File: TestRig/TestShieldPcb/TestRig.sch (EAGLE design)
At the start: 7 parts, among them J1 POWER_JACKPTH, U1 ARDUINO_SHIELDNOHOLES

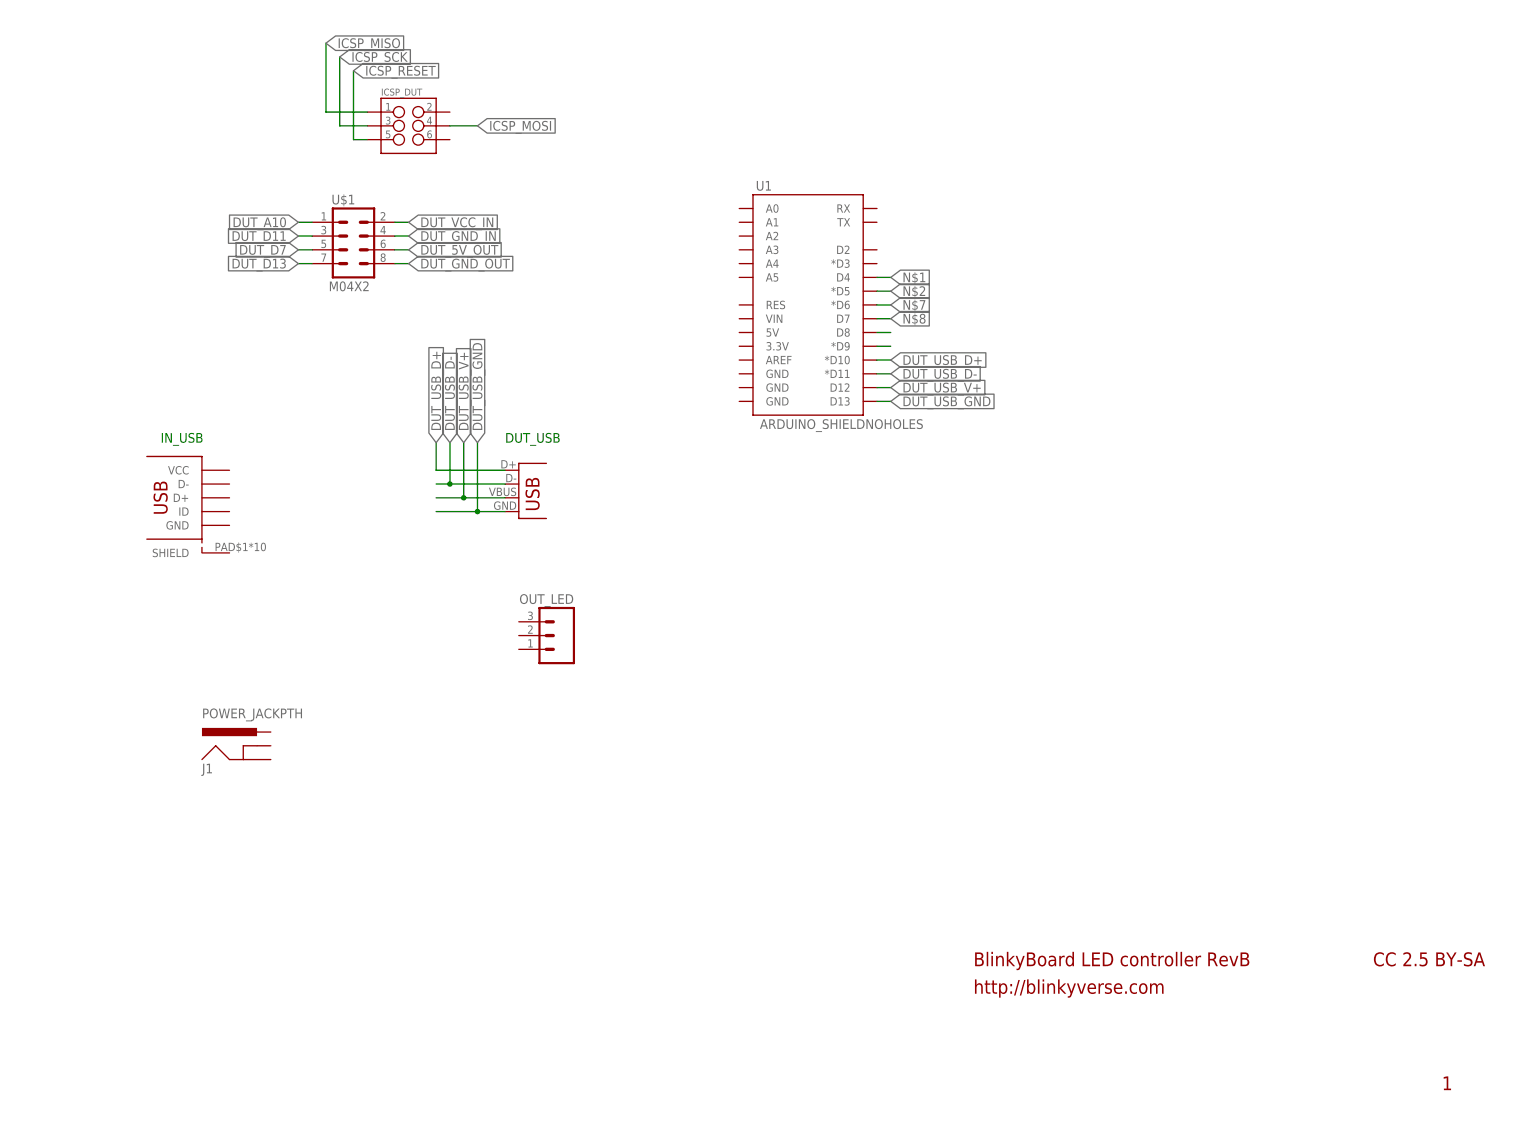
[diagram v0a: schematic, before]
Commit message: Add test shield design
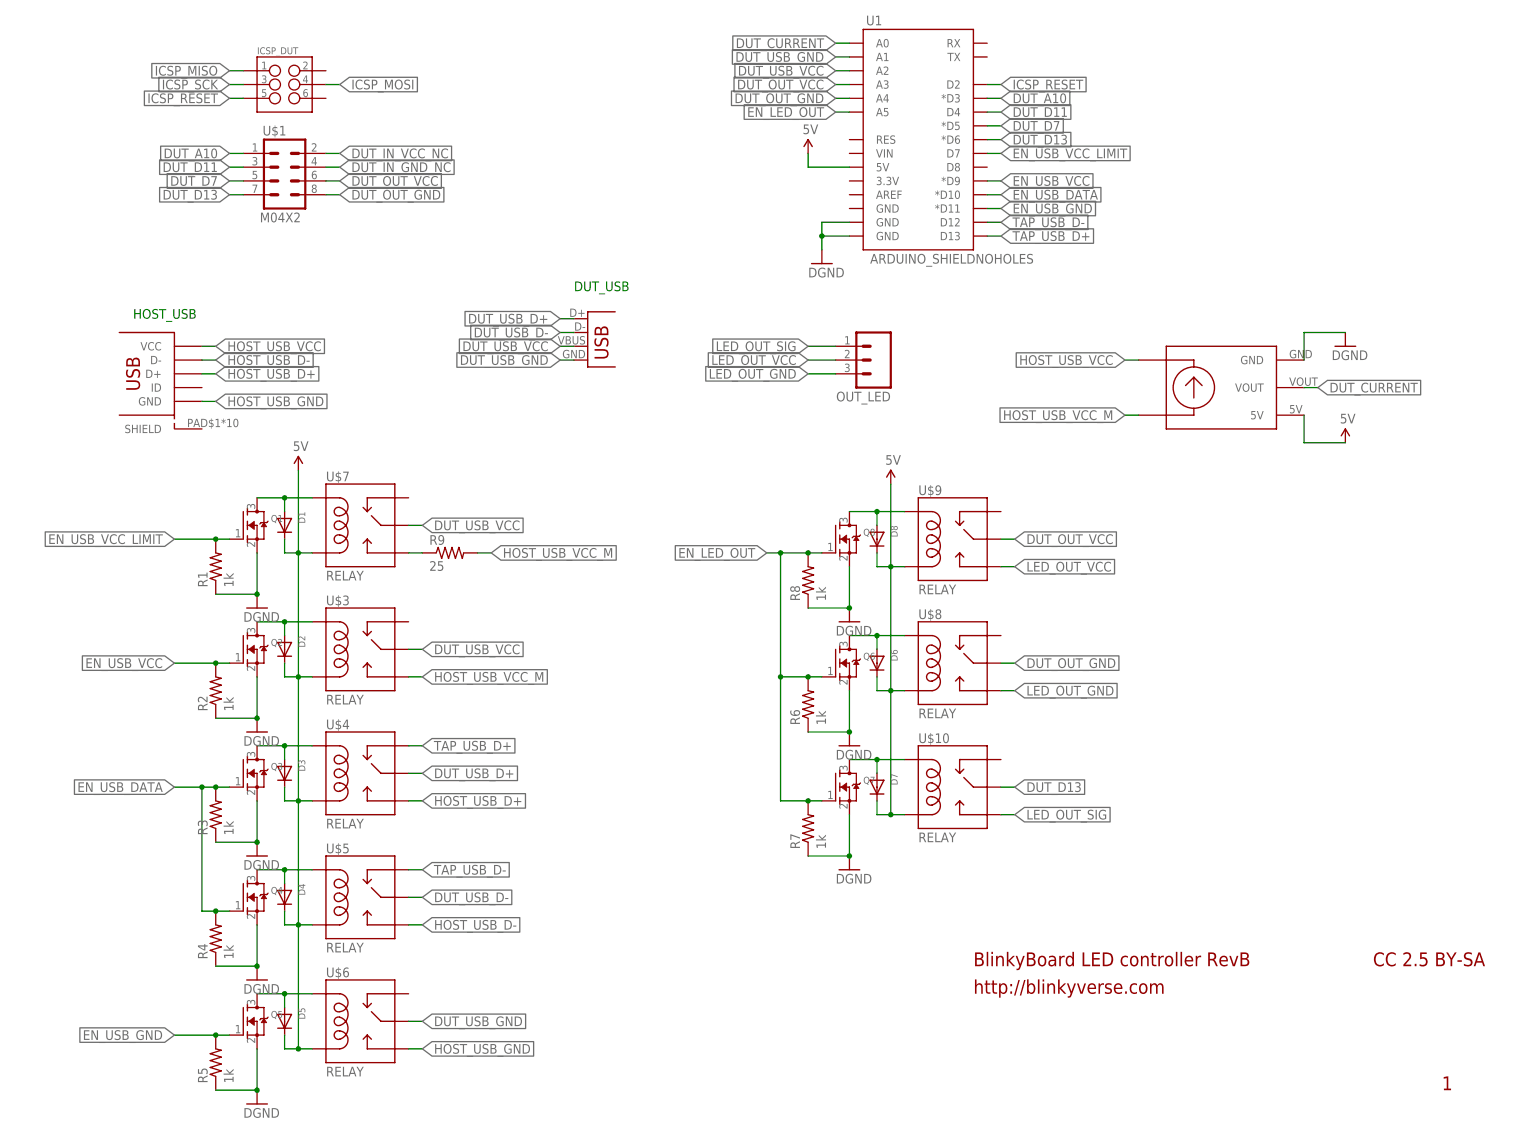
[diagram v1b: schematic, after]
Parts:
- removed J1: POWER_JACKPTH, SparkFun-Connectors:POWER_JACKPTH
- added D1, D2, D3, D4, D5, D6, D7, D8: (no value), adafruit:DIODESOD-523
- added Q1, Q2, Q3, Q4, Q5, Q6, Q7, Q8: (no value), adafruit:MOSFET-NREFLOW
- added R1, R2, R3, R4, R5, R6, R7, R8: 1k, adafruit:R-US_R0603
- added R9: 25, adafruit:R-US_R1210
- added U$10, U$3, U$4, U$5, U$6, U$7, U$8, U$9: RELAY, blinkiverse:RELAY
- added U$11: SPARKFUN_ACS712, blinkiverse:SPARKFUN_ACS712
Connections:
- net DUT_GND_IN renamed DUT_IN_GND_NC
- net DUT_VCC_IN renamed DUT_IN_VCC_NC
- removed net DUT_5V_OUT: U$1.6
- removed net DUT_GND_OUT: U$1.8
- removed net DUT_USB_V+: JP1.VBUS, U1.D12
- removed net N$1: U1.D4
- removed net N$10: U1.*D9
- removed net N$2: U1.*D5
- removed net N$7: U1.*D6
- removed net N$8: U1.D7
- new net 5V: D1.C, D2.C, D3.C, D4.C, D5.C, D6.C, D7.C, D8.C, U$10.COIL2, U$11.5V, U$3.COIL2, U$4.COIL2, U$5.COIL2, U$6.COIL2, U$7.COIL2, U$8.COIL2, U$9.COIL2, U1.5V
- new net DUT_CURRENT: U$11.VOUT, U1.A0
- new net DUT_OUT_GND: U$1.8, U$8.MAIN, U1.A4
- new net DUT_OUT_VCC: U$1.6, U$9.MAIN, U1.A3
- new net DUT_USB_VCC: JP1.VBUS, U$3.MAIN, U$7.MAIN, U1.A2
- new net EN_LED_OUT: Q6.G, Q7.G, Q8.G, R6.2, R7.2, R8.2, U1.A5
- new net EN_USB_DATA: Q3.G, Q4.G, R3.2, R4.2, U1.*D10
- new net EN_USB_GND: Q5.G, R5.2, U1.*D11
- new net EN_USB_VCC: Q2.G, R2.2, U1.*D9
- new net EN_USB_VCC_LIMIT: Q1.G, R1.2, U1.D7
- new net GND: Q1.S, Q2.S, Q3.S, Q4.S, Q5.S, Q6.S, Q7.S, Q8.S, R1.1, R2.1, R3.1, R4.1, R5.1, R6.1, R7.1, R8.1, U$11.GND, U1.GND@0, U1.GND@1
- new net HOST_USB_D+: U$2.D+, U$4.NO
- new net HOST_USB_D-: U$2.D-, U$5.NO
- new net HOST_USB_GND: U$2.GND, U$6.NO
- new net HOST_USB_VCC: U$11.IP+, U$2.VCC
- new net HOST_USB_VCC_M: R9.2, U$11.IP-, U$3.NO
- new net LED_OUT_GND: OUT_LED.3, U$8.NO
- new net LED_OUT_SIG: OUT_LED.1, U$10.NO
- new net LED_OUT_VCC: OUT_LED.2, U$9.NO
- new net N$14: D1.A, Q1.D, U$7.COIL1
- new net N$20: D2.A, Q2.D, U$3.COIL1
- new net N$27: D3.A, Q3.D, U$4.COIL1
- new net N$31: D4.A, Q4.D, U$5.COIL1
- new net N$35: D5.A, Q5.D, U$6.COIL1
- new net N$38: D6.A, Q6.D, U$8.COIL1
- new net N$42: D7.A, Q7.D, U$10.COIL1
- new net N$46: D8.A, Q8.D, U$9.COIL1
- new net TAP_USB_D+: U$4.NC, U1.D13
- new net TAP_USB_D-: U$5.NC, U1.D12
- net DUT_A10: now also U1.*D3
- net DUT_D11: now also U1.D4
- net DUT_D13: now also U$10.MAIN, U1.*D6
- net DUT_D7: now also U1.*D5
- net DUT_USB_D+: now also U$4.MAIN; no longer U1.*D10
- net DUT_USB_D-: now also U$5.MAIN; no longer U1.*D11
- net DUT_USB_GND: now also U$6.MAIN, U1.A1; no longer U1.D13
- net ICSP_RESET: now also U1.D2
- net N$9: now also R9.1, U$7.NO; no longer U1.D8
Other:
- note added: "HOST_USB"
- note removed: "IN_USB"
- moved on the sheet: ICSP_DUT, OUT_LED, U$1, U1

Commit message: RevD of the test shield PCB
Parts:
- removed JP1: USB-A-SMD, SparkFun-Connectors:USB-A-SMD
- added TEST_DUT: M04X2, SparkFun-Connectors:M04X2
- U$1: value M04X2 -> USB; device SparkFun-Connectors:M04X2 -> blinkiverse:USB
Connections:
- new net DUT_USB_SHIELD: U$1.SHIELD, U1.D7
- net DUT_A10: now also TEST_DUT.1; no longer U$1.1
- net DUT_D11: now also TEST_DUT.3; no longer U$1.3
- net DUT_D13: now also TEST_DUT.7; no longer U$1.7
- net DUT_D7: now also TEST_DUT.5; no longer U$1.5
- net DUT_IN_GND_NC: now also TEST_DUT.4; no longer U$1.4
- net DUT_IN_VCC_NC: now also TEST_DUT.2; no longer U$1.2
- net DUT_OUT_GND: now also TEST_DUT.8; no longer U$1.8
- net DUT_OUT_VCC: now also TEST_DUT.6; no longer U$1.6
- net DUT_USB_D+: now also U$1.D+; no longer JP1.D+
- net DUT_USB_D-: now also U$1.D-; no longer JP1.D-
- net DUT_USB_GND: now also U$1.GND; no longer JP1.GND
- net DUT_USB_VCC: now also U$1.VCC; no longer JP1.VBUS
- net EN_USB_VCC_LIMIT: now also U1.D8; no longer U1.D7
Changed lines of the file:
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@@
 <part name="FRAME1" library="frames" deviceset="FRAME_A_L" device=""/>
 <part name="ICSP_DUT" library="SparkFun-Connectors" deviceset="M03X2" device="NO_SILK"/>
-<part name="JP1" library="SparkFun-Connectors" deviceset="USB" device="-A-SMD" value="USB-A-SMD"/>
 <part name="OUT_LED" library="SparkFun-Connectors" deviceset="M03" device="PTH"/>
 <part name="U1" library="SparkFun-Boards" deviceset="ARDUINO_SHIELD" device="NOHOLES"/>
-<part name="U$1" library="SparkFun-Connectors" deviceset="M04X2" device=""/>
+<part name="TEST_DUT" library="SparkFun-Connectors" deviceset="M04X2" device=""/>
 <part name="U$2" library="blinkiverse" deviceset="MICRO_USB" device="SMT+THRUHULE"/>
 <part name="U$3" library="blinkiverse" deviceset="RELAY" device=""/>
@@
 <part name="GND10" library="SparkFun-Aesthetics" deviceset="DGND" device=""/>
 <part name="SUPPLY4" library="SparkFun-Aesthetics" deviceset="5V" device=""/>
+<part name="U$1" library="blinkiverse" deviceset="USB" device=""/>
 </parts>
 <sheets>
@@
 <text x="177.8" y="-30.48" size="2.54" layer="94">CC 2.5 BY-SA</text>
 <text x="190.5" y="-53.34" size="2.54" layer="94">1</text>
-<text x="30.48" y="93.98" size="1.778" layer="91">DUT_USB</text>
+<text x="20.32" y="88.9" size="1.778" layer="91">DUT_USB</text>
 <text x="-50.8" y="88.9" size="1.778" layer="91">HOST_USB</text>
 </plain>
@@
 <instance part="FRAME1" gate="G$2" x="101.6" y="-60.96"/>
 <instance part="ICSP_DUT" gate="G$1" x="-22.86" y="132.08"/>
-<instance part="JP1" gate="G$1" x="33.02" y="81.28"/>
 <instance part="OUT_LED" gate="G$1" x="86.36" y="81.28" rot="R180"/>
 <instance part="U1" gate="G$1" x="93.98" y="121.92"/>
-<instance part="U$1" gate="G$1" x="-22.86" y="114.3"/>
+<instance part="TEST_DUT" gate="G$1" x="-22.86" y="114.3"/>
 <instance part="U$2" gate="G$1" x="-45.72" y="78.74"/>
 <instance part="U$3" gate="G$1" x="-7.62" y="27.94"/>
@@
 <instance part="GND10" gate="G$1" x="172.72" y="83.82"/>
 <instance part="SUPPLY4" gate="G$1" x="172.72" y="66.04"/>
+<instance part="U$1" gate="G$1" x="35.56" y="78.74" rot="MR0"/>
 </instances>
 <busses>
@@
 <net name="DUT_A10" class="0">
 <segment>
-<pinref part="U$1" gate="G$1" pin="1"/>
+<pinref part="TEST_DUT" gate="G$1" pin="1"/>
 <wire x1="-30.48" y1="119.38" x2="-33.02" y2="119.38" width="0.1524" layer="91"/>
 <label x="-33.02" y="119.38" size="1.778" layer="95" rot="R180" xref="yes"/>
@@
 <net name="DUT_D11" class="0">
 <segment>
-<pinref part="U$1" gate="G$1" pin="3"/>
+<pinref part="TEST_DUT" gate="G$1" pin="3"/>
 <wire x1="-33.02" y1="116.84" x2="-30.48" y2="116.84" width="0.1524" layer="91"/>
 <label x="-33.02" y="116.84" size="1.778" layer="95" rot="R180" xref="yes"/>
@@
 <net name="DUT_D7" class="0">
 <segment>
-<pinref part="U$1" gate="G$1" pin="5"/>
+<pinref part="TEST_DUT" gate="G$1" pin="5"/>
 <wire x1="-33.02" y1="114.3" x2="-30.48" y2="114.3" width="0.1524" layer="91"/>
 <label x="-33.02" y="114.3" size="1.778" layer="95" rot="R180" xref="yes"/>
@@
 <net name="DUT_D13" class="0">
 <segment>
-<pinref part="U$1" gate="G$1" pin="7"/>
+<pinref part="TEST_DUT" gate="G$1" pin="7"/>
 <wire x1="-33.02" y1="111.76" x2="-30.48" y2="111.76" width="0.1524" layer="91"/>
 <label x="-33.02" y="111.76" size="1.778" layer="95" rot="R180" xref="yes"/>
@@
 <net name="DUT_IN_VCC_NC" class="0">
 <segment>
-<pinref part="U$1" gate="G$1" pin="2"/>
+<pinref part="TEST_DUT" gate="G$1" pin="2"/>
 <wire x1="-15.24" y1="119.38" x2="-12.7" y2="119.38" width="0.1524" layer="91"/>
 <label x="-12.7" y="119.38" size="1.778" layer="95" xref="yes"/>
@@
 <net name="DUT_IN_GND_NC" class="0">
 <segment>
-<pinref part="U$1" gate="G$1" pin="4"/>
+<pinref part="TEST_DUT" gate="G$1" pin="4"/>
 <wire x1="-15.24" y1="116.84" x2="-12.7" y2="116.84" width="0.1524" layer="91"/>
 <label x="-12.7" y="116.84" size="1.778" layer="95" xref="yes"/>
@@
 <net name="DUT_OUT_GND" class="0">
 <segment>
-<pinref part="U$1" gate="G$1" pin="8"/>
+<pinref part="TEST_DUT" gate="G$1" pin="8"/>
 <wire x1="-15.24" y1="111.76" x2="-12.7" y2="111.76" width="0.1524" layer="91"/>
 <label x="-12.7" y="111.76" size="1.778" layer="95" xref="yes"/>
@@
 <net name="DUT_USB_D+" class="0">
 <segment>
-<pinref part="JP1" gate="G$1" pin="D+"/>
-<wire x1="30.48" y1="88.9" x2="27.94" y2="88.9" width="0.1524" layer="91"/>
-<label x="27.94" y="88.9" size="1.778" layer="95" rot="R180" xref="yes"/>
+<label x="22.86" y="78.74" size="1.778" layer="95" rot="R180" xref="yes"/>
+<pinref part="U$1" gate="G$1" pin="D+"/>
+<wire x1="22.86" y1="78.74" x2="27.94" y2="78.74" width="0.1524" layer="91"/>
 </segment>
 <segment>
@@
 <net name="DUT_USB_D-" class="0">
 <segment>
-<pinref part="JP1" gate="G$1" pin="D-"/>
-<wire x1="30.48" y1="86.36" x2="27.94" y2="86.36" width="0.1524" layer="91"/>
-<label x="27.94" y="86.36" size="1.778" layer="95" rot="R180" xref="yes"/>
+<label x="22.86" y="81.28" size="1.778" layer="95" rot="R180" xref="yes"/>
+<pinref part="U$1" gate="G$1" pin="D-"/>
+<wire x1="22.86" y1="81.28" x2="27.94" y2="81.28" width="0.1524" layer="91"/>
 </segment>
 <segment>
@@
 <net name="DUT_USB_GND" class="0">
 <segment>
-<pinref part="JP1" gate="G$1" pin="GND"/>
-<wire x1="30.48" y1="81.28" x2="27.94" y2="81.28" width="0.1524" layer="91"/>
-<label x="27.94" y="81.28" size="1.778" layer="95" rot="R180" xref="yes"/>
+<label x="22.86" y="76.2" size="1.778" layer="95" rot="R180" xref="yes"/>
+<pinref part="U$1" gate="G$1" pin="GND"/>
+<wire x1="22.86" y1="76.2" x2="27.94" y2="76.2" width="0.1524" layer="91"/>
 </segment>
 <segment>
@@
 </segment>
 <segment>
-<pinref part="JP1" gate="G$1" pin="VBUS"/>
-<wire x1="30.48" y1="83.82" x2="27.94" y2="83.82" width="0.1524" layer="91"/>
-<label x="27.94" y="83.82" size="1.778" layer="95" rot="R180" xref="yes"/>
+<label x="22.86" y="83.82" size="1.778" layer="95" rot="R180" xref="yes"/>
+<pinref part="U$1" gate="G$1" pin="VCC"/>
+<wire x1="22.86" y1="83.82" x2="27.94" y2="83.82" width="0.1524" layer="91"/>
 </segment>
 <segment>
@@
 </segment>
 <segment>
-<pinref part="U1" gate="G$1" pin="D7"/>
-<wire x1="109.22" y1="119.38" x2="106.68" y2="119.38" width="0.1524" layer="91"/>
-<label x="109.22" y="119.38" size="1.778" layer="95" xref="yes"/>
+<label x="109.22" y="116.84" size="1.778" layer="95" xref="yes"/>
+<pinref part="U1" gate="G$1" pin="D8"/>
+<wire x1="106.68" y1="116.84" x2="109.22" y2="116.84" width="0.1524" layer="91"/>
 </segment>
 </net>
@@
 </segment>
 <segment>
-<pinref part="U$1" gate="G$1" pin="6"/>
+<pinref part="TEST_DUT" gate="G$1" pin="6"/>
 <wire x1="-15.24" y1="114.3" x2="-12.7" y2="114.3" width="0.1524" layer="91"/>
 <label x="-12.7" y="114.3" size="1.778" layer="95" xref="yes"/>
@@
 </segment>
 </net>
+<net name="DUT_USB_SHIELD" class="0">
+<segment>
+<pinref part="U$1" gate="G$1" pin="SHIELD"/>
+<wire x1="27.94" y1="71.12" x2="22.86" y2="71.12" width="0.1524" layer="91"/>
+<label x="22.86" y="71.12" size="1.778" layer="95" rot="R180" xref="yes"/>
+</segment>
+<segment>
+<pinref part="U1" gate="G$1" pin="D7"/>
+<wire x1="109.22" y1="119.38" x2="106.68" y2="119.38" width="0.1524" layer="91"/>
+<label x="109.22" y="119.38" size="1.778" layer="95" xref="yes"/>
+</segment>
+</net>

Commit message: Minor updates to test rig
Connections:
- net HOST_USB_VCC: now also U$11.IP-; no longer U$11.IP+
- net HOST_USB_VCC_M: now also U$11.IP+; no longer U$11.IP-
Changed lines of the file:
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@@
 </segment>
 <segment>
-<pinref part="U$11" gate="G$1" pin="IP+"/>
-<wire x1="134.62" y1="81.28" x2="132.08" y2="81.28" width="0.1524" layer="91"/>
-<label x="132.08" y="81.28" size="1.778" layer="95" rot="R180" xref="yes"/>
+<label x="129.54" y="71.12" size="1.778" layer="95" rot="R180" xref="yes"/>
+<pinref part="U$11" gate="G$1" pin="IP-"/>
+<wire x1="129.54" y1="71.12" x2="134.62" y2="71.12" width="0.1524" layer="91"/>
 </segment>
 </net>
@@
 </segment>
 <segment>
-<pinref part="U$11" gate="G$1" pin="IP-"/>
-<wire x1="132.08" y1="71.12" x2="134.62" y2="71.12" width="0.1524" layer="91"/>
-<label x="132.08" y="71.12" size="1.778" layer="95" rot="R180" xref="yes"/>
-</segment>
-</net>
+<label x="129.54" y="81.28" size="1.778" layer="95" rot="R180" xref="yes"/>
+<pinref part="U$11" gate="G$1" pin="IP+"/>
+<wire x1="134.62" y1="81.28" x2="129.54" y2="81.28" width="0.1524" layer="91"/>
+</segment>
+</net>

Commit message: Test rig update: programming, current measurement functional
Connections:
- net DUT_A10: now also U1.TX; no longer U1.*D3
- net ICSP_RESET: now also U1.RX; no longer U1.D2
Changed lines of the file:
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@@
 </segment>
 <segment>
-<pinref part="U1" gate="G$1" pin="D2"/>
-<wire x1="106.68" y1="132.08" x2="109.22" y2="132.08" width="0.1524" layer="91"/>
-<label x="109.22" y="132.08" size="1.778" layer="95" xref="yes"/>
+<label x="109.22" y="139.7" size="1.778" layer="95" xref="yes"/>
+<pinref part="U1" gate="G$1" pin="RX"/>
+<wire x1="109.22" y1="139.7" x2="106.68" y2="139.7" width="0.1524" layer="91"/>
 </segment>
 </net>
@@
 </segment>
 <segment>
-<pinref part="U1" gate="G$1" pin="*D3"/>
-<wire x1="109.22" y1="129.54" x2="106.68" y2="129.54" width="0.1524" layer="91"/>
-<label x="109.22" y="129.54" size="1.778" layer="95" xref="yes"/>
+<label x="109.22" y="137.16" size="1.778" layer="95" xref="yes"/>
+<pinref part="U1" gate="G$1" pin="TX"/>
+<wire x1="109.22" y1="137.16" x2="106.68" y2="137.16" width="0.1524" layer="91"/>
 </segment>
 </net>
